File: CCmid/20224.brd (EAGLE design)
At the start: 17.1 x 10.8 mm, 10 parts, among them J1 PST1,0/2-3,5, J2 PST1,0/2-3,5, U3 A6

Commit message: CCmid: referance values
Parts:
- removed C13, C9: 1uF, C-C:C0805(2012)
- removed D3: SQ4, D-SBR:SMA
- removed U3: A6, U-Linear:SOT23-5
- added C1, C2: 1uF, C-C:C0805(2012)
- added D2: SQ4, D-SBR:SMA
- added U1: A6, U-Linear:SOT23-5
- moved J2 3.18 mm to (17.8, 3.17)
- moved R1 2.54 mm to (14.9, 6.99)
- moved D1 2.04 mm to (7.37, 4.83), flipped to the bottom
- moved L1 0.63 mm to (10.7, 5.21)
- moved R2 0.52 mm to (4.45, 8.38)
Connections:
- net +CH: now also C2.1, U1.4; no longer C9.1, U3.4
- net -CH: now also C2.2; no longer C9.2
- net 0V: now also C1.2, U1.2; no longer C13.2, U3.2
- net IO3: now also U1.3; no longer U3.3
- net N$3: now also D2.A, U1.1; no longer D3.A, U3.1
- net VIN: now also C1.1, D2.K, U1.5; no longer C13.1, D3.K, U3.5
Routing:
- net +CH: track 0.00 -> 31.0 mm, vias 0 -> 1
- net N$3: track 0.00 -> 15.9 mm, vias 0 -> 1
- net -CH: track 0.00 -> 13.4 mm
- net VIN: track 0.00 -> 10.5 mm
- net IO3: track 0.00 -> 4.44 mm
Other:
- board size 17.1 x 10.8 mm -> 20.3 x 10.8 mm

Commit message: CCmid: ic is obsolete
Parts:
- removed C2: 1uF, C-C:C0805(2012)
- removed R2: 3.74k, R-C:C0805(2012)
- removed U1: A6, U-Linear:SOT23-5
- added K1: PC357NJ0000F, K-OPT:SMD4
- added U2: AL8862, U-LED:SOIC8EP
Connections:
- removed net IO3: R2.2, U1.3
- new net N$1: K1.4, U2.8
- net +CH: now also U2.1; no longer C2.1, U1.4
- net -CH: no longer C2.2
- net 0V: now also K1.3, U2.2, U2.7, U2.EP; no longer R2.1, U1.2
- net N$3: now also U2.5, U2.6; no longer U1.1
- net VIN: now also U2.4; no longer U1.5
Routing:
- net -CH: track 13.4 -> 8.71 mm
- net IO3: track 4.44 -> 0.00 mm
- net +CH: track 31.0 -> 29.8 mm
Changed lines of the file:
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@@
 </autorouter>
 <elements>
-<element name="U1" library="U-Linear" package="SOT23-5" value="A6" x="10.922" y="8.001" smashed="yes" rot="MR90">
-<attribute name="NAME" x="8.763" y="9.525" size="0.6096" layer="26" rot="MR270"/>
-</element>
 <element name="L1" library="L-PWR" package="L2424" value="33uH" x="10.668" y="5.207" smashed="yes" rot="R90">
 <attribute name="NAME" x="9.0191" y="1.8219" size="0.6096" layer="25" rot="R180"/>
@@
 <attribute name="NAME" x="15.03" y="4.223" size="0.6096" layer="26" ratio="10" rot="MR180"/>
 </element>
-<element name="C2" library="C-C" package="C0805(2012)" value="1uF" x="4.572" y="5.715" smashed="yes" rot="MR90">
-<attribute name="NAME" x="5.08" y="3.048" size="0.6096" layer="26" rot="MR0"/>
-<attribute name="VALUE" x="4.318" y="4.826" size="0.4064" layer="28" rot="MR90"/>
-</element>
 <element name="R1" library="R-C" package="C1210(3225)" value="0.30" x="14.859" y="6.985" smashed="yes" rot="MR270">
 <attribute name="NAME" x="17.018" y="5.588" size="0.6096" layer="26" rot="MR270"/>
 <attribute name="VALUE" x="15.113" y="8.001" size="0.4064" layer="28" rot="MR270"/>
-</element>
-<element name="R2" library="R-C" package="C0805(2012)" value="3.74k" x="4.445" y="8.382" smashed="yes" rot="MR180">
-<attribute name="NAME" x="1.905" y="8.255" size="0.6096" layer="26" rot="MR90"/>
-<attribute name="VALUE" x="3.556" y="8.636" size="0.4064" layer="28" rot="MR180"/>
 </element>
 <element name="C1" library="C-C" package="C0805(2012)" value="1uF" x="11.557" y="5.334" smashed="yes" rot="MR0">
@@
 <attribute name="NAME" x="6.052" y="1.492" size="0.6096" layer="26" ratio="10" rot="MR0"/>
 </element>
+<element name="U2" library="U-LED" package="SOIC8EP" value="AL8862" x="-3.81" y="3.81"/>
+<element name="K1" library="K-OPT" package="SMD4" value="PC357NJ0000F" x="-9.525" y="4.445"/>
 </elements>
 <signals>
@@
 <via x="2.667" y="4.953" extent="1-16" drill="0.4064"/>
 <via x="17.145" y="1.524" extent="1-16" drill="0.4064"/>
-<contactref element="R2" pad="1"/>
-<contactref element="U1" pad="2"/>
 <contactref element="C1" pad="2"/>
 <contactref element="J2" pad="2"/>
@@
 <via x="10.922" y="9.398" extent="1-16" drill="0.4064"/>
 <via x="1.651" y="9.271" extent="1-16" drill="0.4064"/>
+<contactref element="U2" pad="2"/>
+<contactref element="U2" pad="7"/>
+<contactref element="U2" pad="EP"/>
+<contactref element="K1" pad="3"/>
+<wire x1="13.716" y1="4.064" x2="17.78" y2="6.675" width="0" layer="19" extent="1-1"/>
+<wire x1="10.58" y1="5.334" x2="13.716" y2="4.064" width="0" layer="19" extent="16-16"/>
+<wire x1="10.922" y1="9.398" x2="10.58" y2="5.334" width="0" layer="19" extent="16-16"/>
+<wire x1="17.145" y1="1.524" x2="13.716" y2="4.064" width="0" layer="19" extent="1-1"/>
+<wire x1="2.667" y1="4.953" x2="10.58" y2="5.334" width="0" layer="19" extent="16-16"/>
+<wire x1="3.302" y1="1.524" x2="2.667" y2="4.953" width="0" layer="19" extent="1-1"/>
+<wire x1="1.651" y1="9.271" x2="2.667" y2="4.953" width="0" layer="19" extent="1-1"/>
+<wire x1="-3.81" y1="3.81" x2="2.667" y2="4.953" width="0" layer="19" extent="1-1"/>
+<wire x1="-4.445" y1="1.27" x2="-3.81" y2="3.81" width="0" layer="19" extent="1-1"/>
+<wire x1="-4.445" y1="6.35" x2="-3.81" y2="3.81" width="0" layer="19" extent="1-1"/>
+<wire x1="-8.255" y1="7.595" x2="-4.445" y2="6.35" width="0" layer="19" extent="1-1"/>
 </signal>
 <signal name="VIN">
 <contactref element="R1" pad="2"/>
-<contactref element="U1" pad="5"/>
 <contactref element="D2" pad="K"/>
 <contactref element="C1" pad="1"/>
@@
 <wire x1="13.84" y1="5.585" x2="13.589" y2="5.334" width="0.8128" layer="16"/>
 <wire x1="13.589" y1="5.334" x2="12.534" y2="5.334" width="0.8128" layer="16"/>
-<wire x1="12.2221" y1="7.051" x2="12.2221" y2="6.7009" width="0.254" layer="16"/>
 <wire x1="12.2221" y1="6.7009" x2="12.534" y2="6.389" width="0.254" layer="16"/>
 <wire x1="12.534" y1="5.334" x2="12.534" y2="6.389" width="0.254" layer="16"/>
-</signal>
-<signal name="IO3">
-<contactref element="U1" pad="3"/>
-<contactref element="R2" pad="2"/>
-<wire x1="5.422" y1="8.382" x2="6.223" y2="8.382" width="0.254" layer="16"/>
-<wire x1="6.223" y1="8.382" x2="6.35" y2="8.509" width="0.254" layer="16"/>
-<wire x1="6.35" y1="8.509" x2="8.509" y2="8.509" width="0.254" layer="16"/>
-<wire x1="8.509" y1="8.509" x2="8.951" y2="8.951" width="0.254" layer="16"/>
-<wire x1="9.6219" y1="8.951" x2="8.951" y2="8.951" width="0.254" layer="16"/>
+<contactref element="U2" pad="4"/>
+<wire x1="-1.905" y1="1.27" x2="12.534" y2="5.334" width="0" layer="19" extent="1-16"/>
 </signal>
 <signal name="+CH">
-<contactref element="U1" pad="4"/>
 <contactref element="R1" pad="1"/>
-<contactref element="C2" pad="1"/>
 <contactref element="J1" pad="1"/>
 <contactref element="D1" pad="K"/>
@@
 <wire x1="4.953" y1="5.207" x2="2.921" y2="3.175" width="0.8128" layer="1"/>
 <wire x1="2.921" y1="3.175" x2="2.54" y2="3.175" width="0.8128" layer="1"/>
-<wire x1="4.572" y1="4.738" x2="4.103" y2="4.738" width="0.8128" layer="16"/>
 <wire x1="4.103" y1="4.738" x2="2.54" y2="3.175" width="0.8128" layer="16"/>
 <wire x1="7.366" y1="2.826" x2="6.89" y2="2.826" width="0.8128" layer="16"/>
@@
 <wire x1="4.572" y1="2.667" x2="3.048" y2="2.667" width="0.8128" layer="16"/>
 <wire x1="3.048" y1="2.667" x2="2.54" y2="3.175" width="0.8128" layer="16"/>
-<wire x1="12.2221" y1="8.951" x2="13.02" y2="8.951" width="0.254" layer="16"/>
 <wire x1="13.02" y1="8.951" x2="13.586" y2="8.385" width="0.254" layer="16"/>
 <wire x1="14.859" y1="8.385" x2="13.586" y2="8.385" width="0.254" layer="16"/>
+<contactref element="U2" pad="1"/>
+<wire x1="-5.715" y1="1.27" x2="2.54" y2="3.175" width="0" layer="19" extent="1-1"/>
 </signal>
 <signal name="-CH">
-<contactref element="C2" pad="2"/>
 <contactref element="L1" pad="1"/>
 <contactref element="J1" pad="2"/>
@@
 <wire x1="10.668" y1="7.557" x2="3.422" y2="7.557" width="0.8128" layer="1"/>
 <wire x1="3.422" y1="7.557" x2="2.54" y2="6.675" width="0.8128" layer="1"/>
-<wire x1="4.572" y1="6.692" x2="2.557" y2="6.692" width="0.8128" layer="16"/>
 <wire x1="2.557" y1="6.692" x2="2.54" y2="6.675" width="0.8128" layer="16"/>
-<wire x1="4.572" y1="6.692" x2="7.232" y2="6.692" width="0.8128" layer="16"/>
 <wire x1="7.232" y1="6.692" x2="7.366" y2="6.826" width="0.8128" layer="16"/>
+<wire x1="10.668" y1="7.557" x2="7.366" y2="6.826" width="0" layer="19" extent="1-16"/>
 </signal>
 <signal name="N$3">
-<contactref element="U1" pad="1"/>
 <contactref element="L1" pad="2"/>
 <contactref element="D2" pad="A"/>
-<wire x1="9.6219" y1="7.051" x2="9.21" y2="7.051" width="0.6096" layer="16"/>
 <wire x1="9.21" y1="7.051" x2="9.017" y2="6.858" width="0.6096" layer="16"/>
 <wire x1="9.017" y1="6.858" x2="9.017" y2="5.461" width="0.8128" layer="16"/>
@@
 <wire x1="9.017" y1="2.857" x2="9.017" y2="4.191" width="0.8128" layer="16"/>
 <wire x1="9.017" y1="4.191" x2="8.382" y2="4.826" width="0.8128" layer="16"/>
+<contactref element="U2" pad="5"/>
+<contactref element="U2" pad="6"/>
+<wire x1="-1.905" y1="6.35" x2="5.715" y2="3.81" width="0" layer="19" extent="1-16"/>
+<wire x1="-3.175" y1="6.35" x2="-1.905" y2="6.35" width="0" layer="19" extent="1-1"/>
+</signal>
+<signal name="N$1">
+<contactref element="K1" pad="4"/>
+<contactref element="U2" pad="8"/>
+<wire x1="-5.715" y1="6.35" x2="-10.795" y2="7.595" width="0" layer="19" extent="1-1"/>
 </signal>
 </signals>

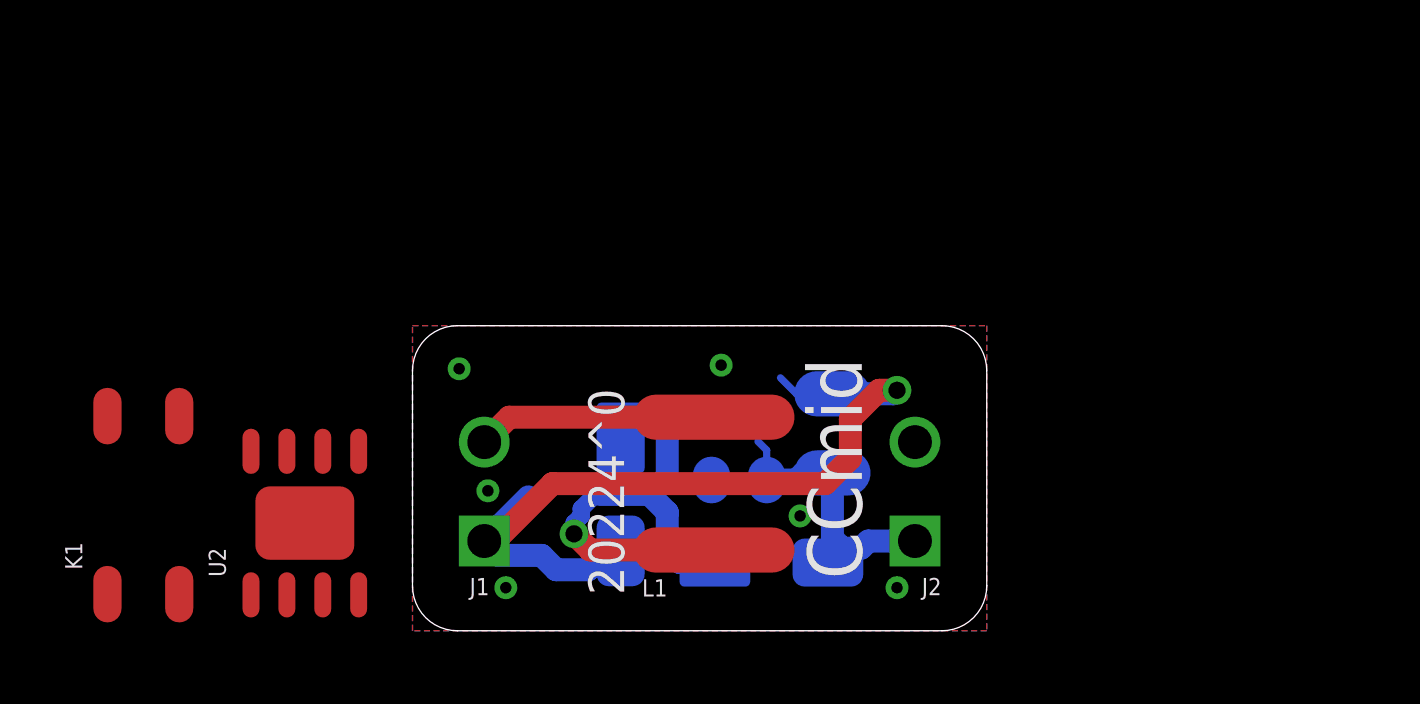
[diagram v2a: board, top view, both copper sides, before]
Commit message: CCmid: fix obsolete part, set up for bat chrg
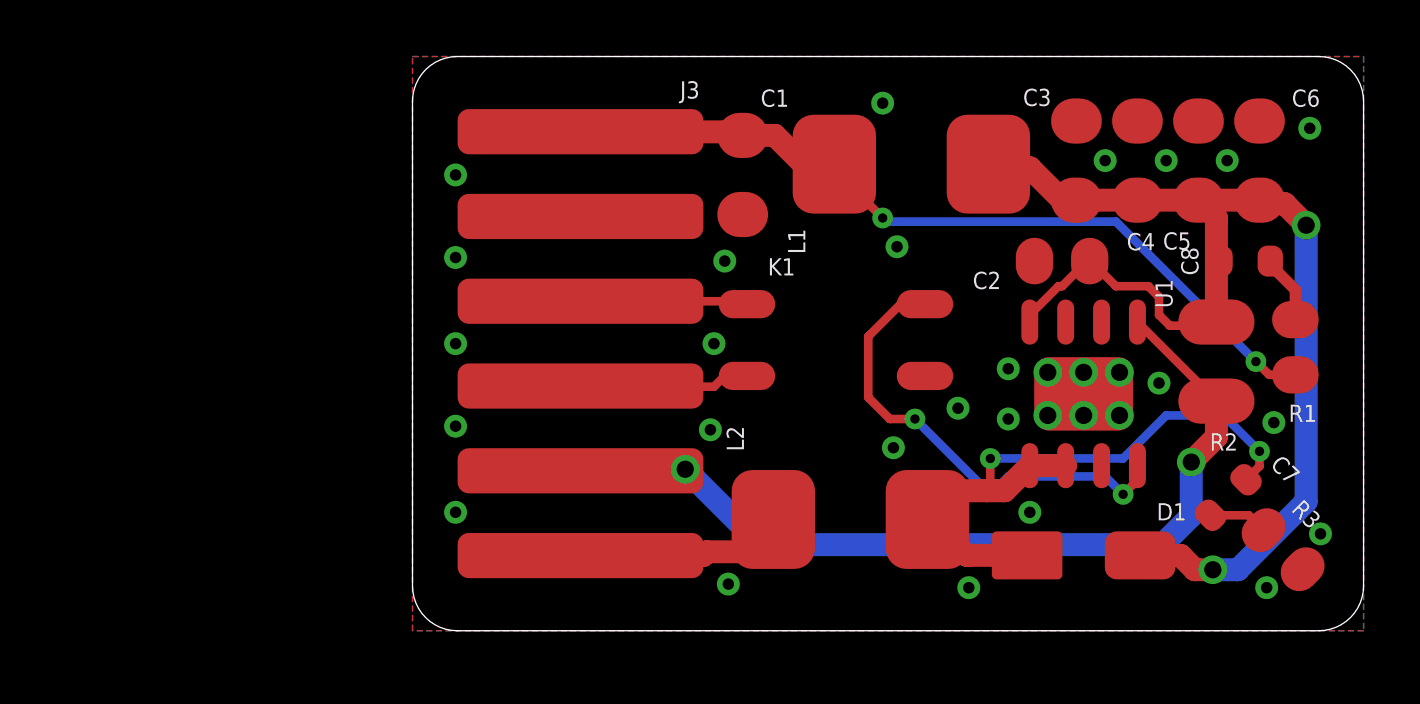
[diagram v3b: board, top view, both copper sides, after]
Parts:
- removed D2: SQ4, D-SBR:SMA
- removed J1, J2: PST1,0/2-3,5, J-HDR3.5mm:MCV2
- removed U2: AL8862, U-LED:SOIC8EP
- added C2: .1uF, C-C:C0805(2012)
- added C3, C4, C5, C6: 10uF, C-C:C1206(3216)
- added C7: 470pF, C-C:C0603(1608)
- added C8: 680pF, C-C:C0603(1608)
- added J3: 9296006, J-PokeIn:06
- added L2: SRP7050TA-680M, L-PWR:L2626
- added R2: 0.15, R-C:C1210(3225)
- added R3: 3.3, R-C:C0805(2012)
- added U1: AL8862, U-LED:SOIC8EP
- C1: value 1uF -> 10uF; device C-C:C0805(2012) -> C-C:C1206(3216)
- D1: value JG -> SQ4; device D-TVS:SMA -> D-SBR:SMA
- L1: value 33uH -> SRP7050TA-680M; device L-PWR:L2424 -> L-PWR:L2626
- R1: value 0.30 -> 482; device R-C:C1210(3225) -> R-C:C0805(2012)
- moved K1 25.2 mm to (15.0, 10.3), turned to 270 degrees
- moved R1 16.7 mm to (31.2, 10.0), flipped to the top, turned to 90 degrees
- moved D1 16.5 mm to (23.7, 2.67), flipped to the top, turned to 180 degrees
- moved L1 13.3 mm to (17.7, 16.5), turned to 180 degrees
- moved C1 10.8 mm to (11.7, 16.1), flipped to the top, turned to 270 degrees
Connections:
- removed net VIN: C1.1, D2.K, J2.1, R1.2, U2.4
- new net 0: C2.1, C3.1, C4.1, C5.1, C6.1, C8.1, D1.K, L1.2, R2.2, U1.4
- new net N$2: J3.3, K1.1
- new net N$4: J3.4, K1.2
- new net N$5: C1.1, J3.1, L1.1, R1.1
- new net N$6: C7.2, R3.2
- new net N$7: C8.2, R1.2
- net +CH: now also J3.5, R2.1, U1.1; no longer D1.K, J1.1, R1.1, U2.1
- net -CH: now also J3.6, L2.2; no longer D1.A, J1.2, L1.1
- net 0V: now also C2.2, C3.2, C4.2, C5.2, C6.2, J3.2, R3.1, U1.2, U1.7, U1.EP; no longer J2.2, U2.2, U2.7, U2.EP
- net N$1: now also U1.8; no longer U2.8
- net N$3: now also C7.1, D1.A, L2.1, U1.5, U1.6; no longer D2.A, L1.2, U2.5, U2.6
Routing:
- net 0: track 0.00 -> 43.0 mm, vias 0 -> 2
- net N$5: track 0.00 -> 29.0 mm, vias 0 -> 2
- net N$1: track 0.00 -> 16.5 mm, vias 0 -> 2
- net VIN: track 10.1 -> 0.00 mm
- net N$3: track 15.5 -> 22.8 mm, vias 1 -> 2
- net N$4: track 0.00 -> 6.06 mm
- net N$2: track 0.00 -> 5.93 mm
- net N$7: track 0.00 -> 2.41 mm
- net N$6: track 0.00 -> 2.10 mm
- net +CH: track 29.8 -> 31.6 mm, vias 1 -> 2
- net -CH: track 8.71 -> 7.35 mm
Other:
- board size 20.3 x 10.8 mm -> 33.7 x 20.3 mm
- board text added: "20224^1"
- board text removed: "20224^0"

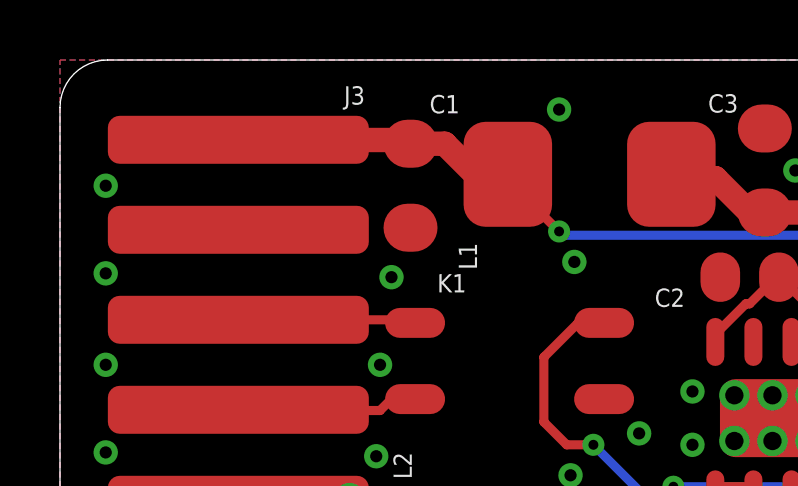
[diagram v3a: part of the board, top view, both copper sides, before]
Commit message: CCmid: rm facing 10uF, add tvs, check inrush
that bulk voltage peak is a problem when I use the inductor to limit inrush
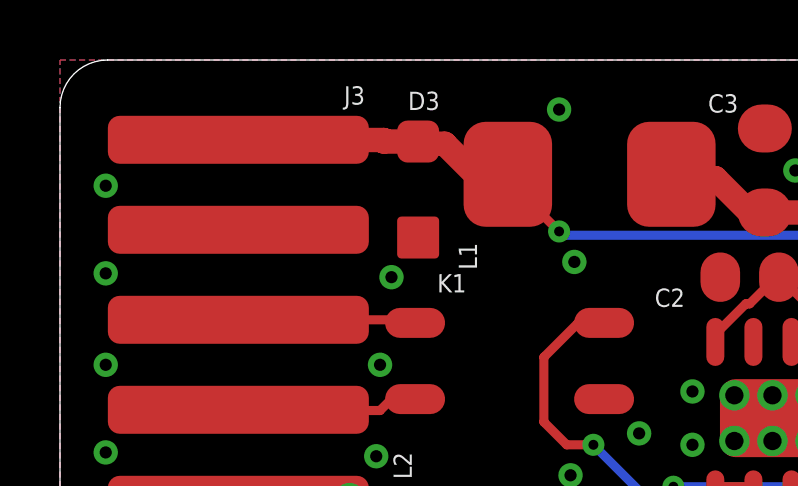
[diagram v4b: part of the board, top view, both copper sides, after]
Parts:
- removed C1: 10uF, C-C:C1206(3216)
- added D3: SMF36CA, D-TVS:SOD123
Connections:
- net 0 renamed BULK
- net 0V: now also D3.A; no longer C1.2
- net N$5: now also D3.C; no longer C1.1
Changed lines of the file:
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@@
 <layer number="19" name="Unrouted" color="6" fill="1" visible="yes" active="yes"/>
 <layer number="20" name="Dimension" color="15" fill="1" visible="yes" active="yes"/>
-<layer number="21" name="tPlace" color="7" fill="1" visible="yes" active="yes"/>
-<layer number="22" name="bPlace" color="7" fill="1" visible="yes" active="yes"/>
+<layer number="21" name="tPlace" color="7" fill="1" visible="no" active="yes"/>
+<layer number="22" name="bPlace" color="7" fill="1" visible="no" active="yes"/>
 <layer number="23" name="tOrigins" color="15" fill="1" visible="yes" active="yes"/>
 <layer number="24" name="bOrigins" color="15" fill="1" visible="yes" active="yes"/>
@@
 <attribute name="VALUE" x="30.226" y="15.621" size="0.4064" layer="27" rot="R90"/>
 </element>
-<element name="C1" library="C-C" package="C1206(3216)" value="10uF" x="11.684" y="16.129" smashed="yes" rot="R270">
-<attribute name="NAME" x="12.319" y="18.542" size="0.6096" layer="25"/>
-<attribute name="VALUE" x="11.43" y="17.145" size="0.4064" layer="27" rot="R270"/>
-</element>
 <element name="C7" library="C-C" package="C0603(1608)" value="470pF" x="28.8662" y="4.714409375" smashed="yes" rot="R225">
 <attribute name="NAME" x="31.458803125" y="5.563565625" size="0.6096" layer="25" rot="R135"/>
@@
 <attribute name="NAME" x="32.004" y="8.001" size="0.6096" layer="25" rot="R180"/>
 <attribute name="VALUE" x="31.496" y="9.144" size="0.4064" layer="27" rot="R90"/>
+</element>
+<element name="D3" library="D-TVS" package="SOD123" value="SMF36CA" x="11.938" y="16.002" smashed="yes" rot="R270">
+<attribute name="NAME" x="11.6" y="18.653" size="0.6096" layer="25"/>
 </element>
 </elements>
@@
 <contactref element="K1" pad="3"/>
 <contactref element="J3" pad="2"/>
-<contactref element="C1" pad="2"/>
 <contactref element="C3" pad="2"/>
 <contactref element="C4" pad="2"/>
@@
 <via x="23.749" y="7.62" extent="1-16" drill="0.6096"/>
 <via x="21.844" y="4.191" extent="1-16" drill="0.4064"/>
-</signal>
-<signal name="0">
+<contactref element="D3" pad="A"/>
+</signal>
+<signal name="BULK">
 <contactref element="R2" pad="2"/>
 <contactref element="D1" pad="K"/>
@@
 <signal name="N$5">
 <contactref element="J3" pad="1"/>
-<contactref element="C1" pad="1"/>
 <contactref element="L1" pad="1"/>
 <contactref element="R1" pad="1"/>
 <wire x1="14.928" y1="16.51" x2="13.843" y2="16.51" width="0.8128" layer="1"/>
 <wire x1="13.843" y1="16.51" x2="12.824" y2="17.529" width="0.8128" layer="1"/>
-<wire x1="11.684" y1="17.529" x2="12.824" y2="17.529" width="0.8128" layer="1"/>
-<wire x1="11.684" y1="17.529" x2="11.173" y2="17.529" width="0.8128" layer="1"/>
-<wire x1="11.173" y1="17.529" x2="11.049" y2="17.653" width="0.8128" layer="1"/>
-<wire x1="11.049" y1="17.653" x2="5.952" y2="17.653" width="0.8128" layer="1"/>
-<wire x1="5.952" y1="17.653" x2="5.945" y2="17.66" width="0.8128" layer="1"/>
 <wire x1="31.242" y1="9.056" x2="30.314" y2="9.056" width="0.3048" layer="1"/>
 <wire x1="30.314" y1="9.056" x2="29.845" y2="9.525" width="0.3048" layer="1"/>
@@
 <wire x1="16.129" y1="15.113" x2="16.129" y2="15.309" width="0.3048" layer="1"/>
 <wire x1="16.129" y1="15.309" x2="14.928" y2="16.51" width="0.3048" layer="1"/>
+<contactref element="D3" pad="C"/>
+<wire x1="12.824" y1="17.529" x2="11.938" y2="17.529" width="0.8128" layer="1"/>
+<wire x1="11.938" y1="17.529" x2="11.938" y2="17.602" width="0.8128" layer="1"/>
+<wire x1="11.938" y1="17.602" x2="10.795" y2="17.602" width="0.8128" layer="1"/>
+<wire x1="10.795" y1="17.602" x2="10.795" y2="17.653" width="0.8128" layer="1"/>
+<wire x1="10.795" y1="17.653" x2="5.945" y2="17.653" width="0.8128" layer="1"/>
+<wire x1="5.945" y1="17.653" x2="5.945" y2="17.66" width="0.8128" layer="1"/>
 </signal>
 <signal name="N$6">
